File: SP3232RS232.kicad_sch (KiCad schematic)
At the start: 14 parts, among them J13 RSS232Out, J14 RSS232In, U4 MAX3232

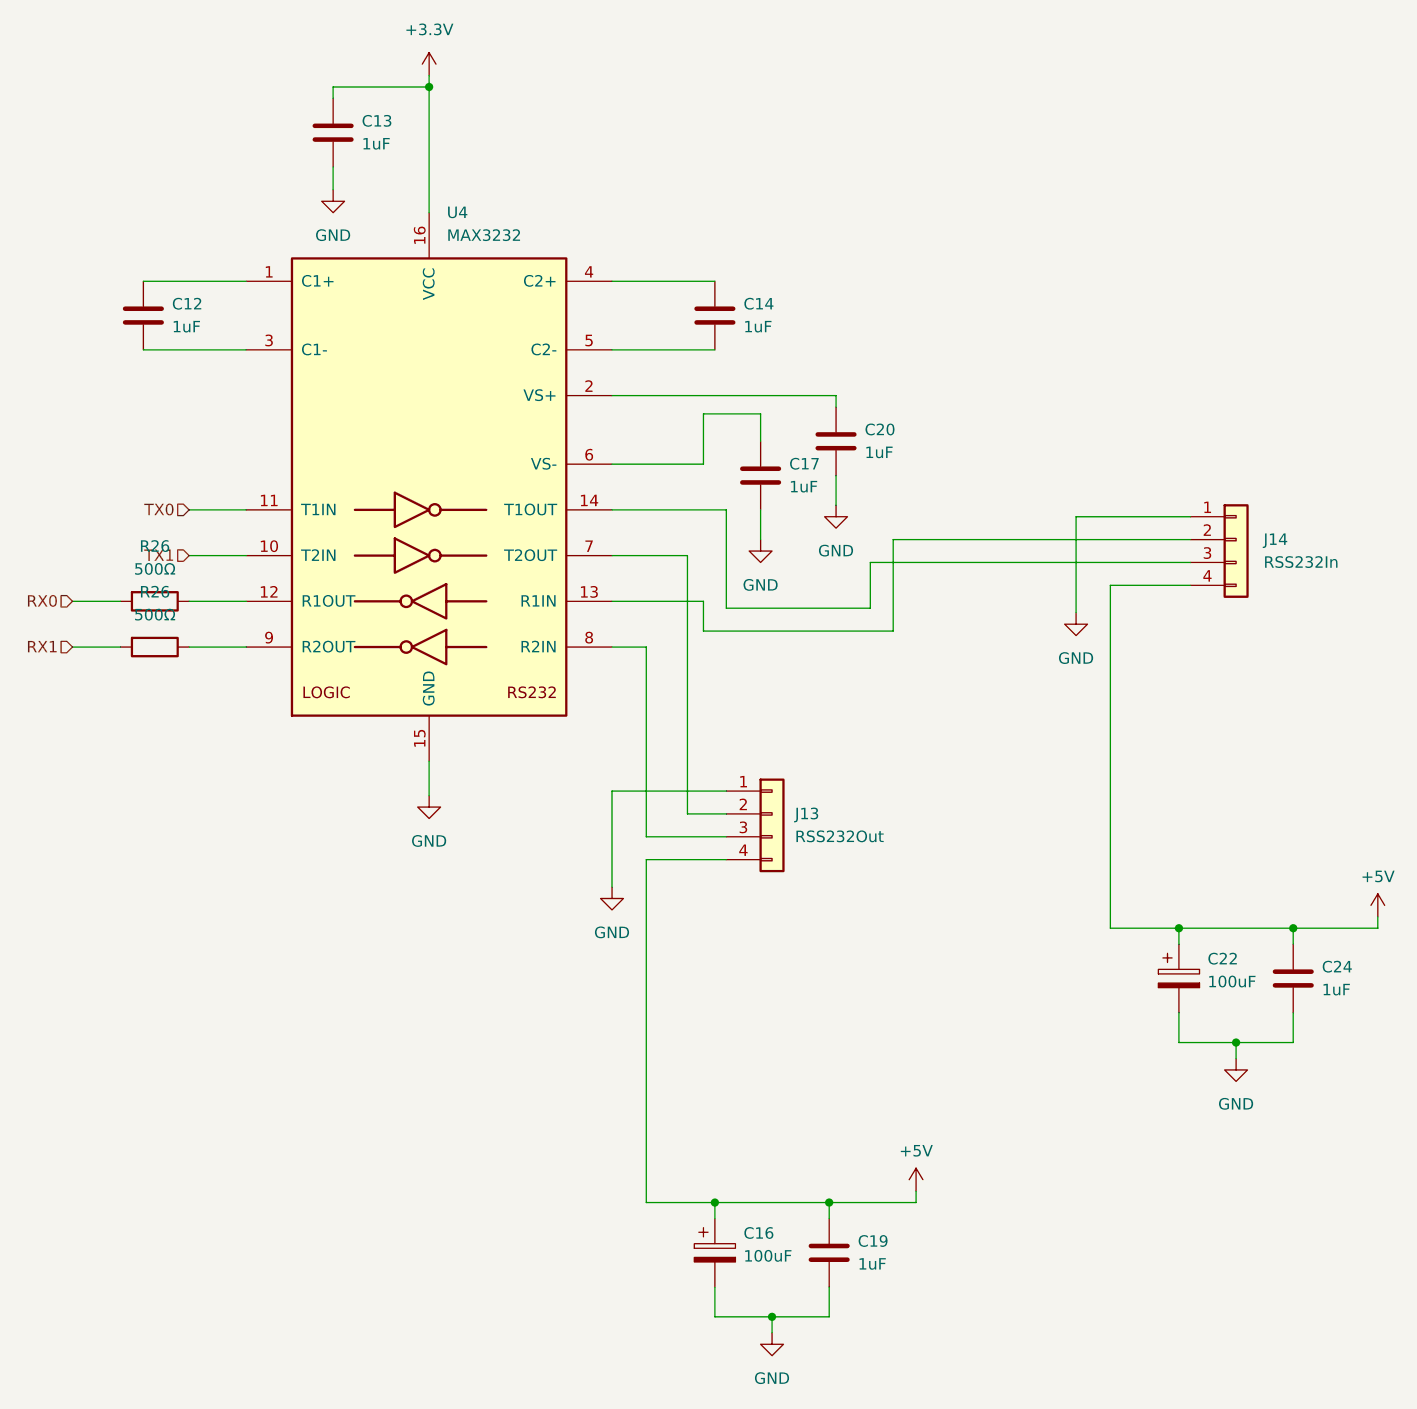
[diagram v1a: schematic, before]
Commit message: Finished schematic. Move to PCB.
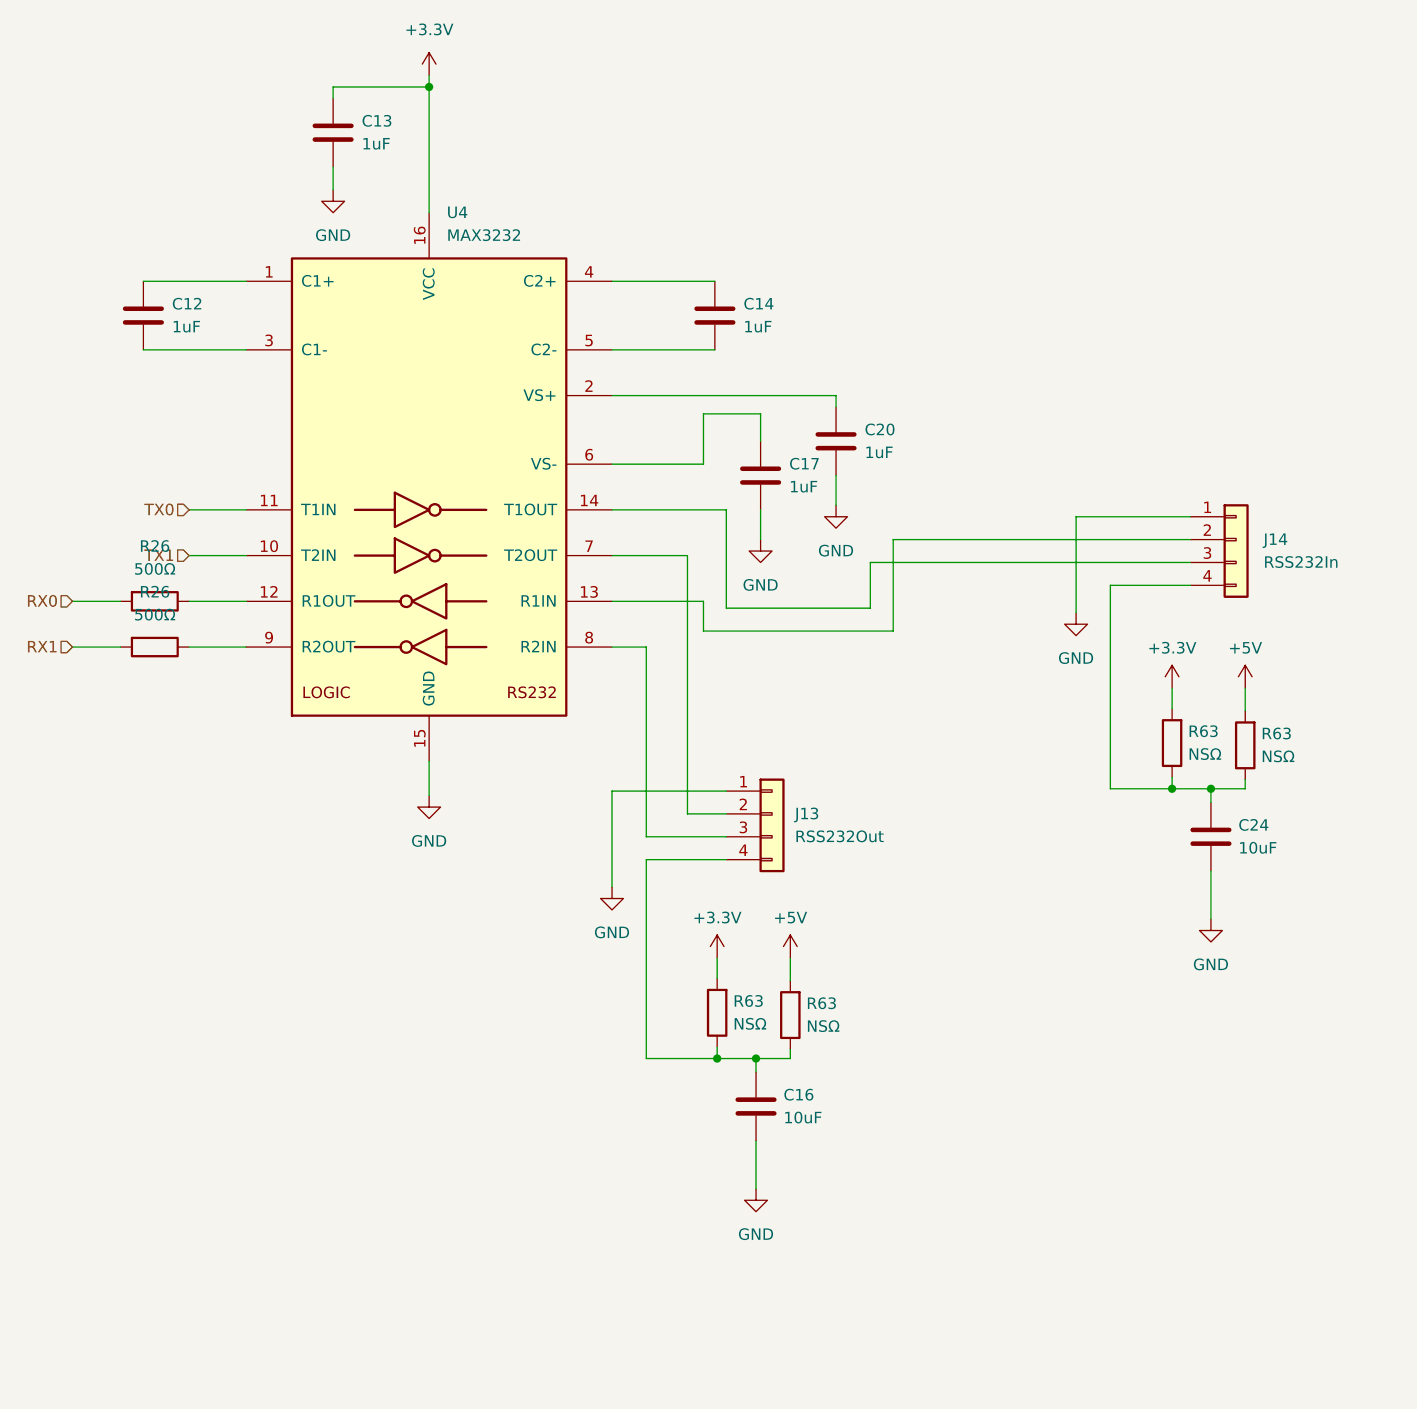
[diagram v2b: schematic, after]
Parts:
- removed C16, C22: 100uF, Capacitor_SMD:CP_Elec_8x11.9, symbol Device:C_Polarized
- removed C19: 1uF, Capacitor_SMD:C_0805_2012Metric, symbol Device:C
- added C16: 10uF, Capacitor_SMD:C_0805_2012Metric, symbol Device:C
- added R63 (x4): NSΩ, Resistor_SMD:R_0805_2012Metric, symbol Device:R
- C24: value 1uF -> 10uF
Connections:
- net +3.3V: now also R63.2, R63.2
- net +5V: now also R63.2, R63.2; no longer C24.1, J13.4 (Pin_4), J14.4 (Pin_4)
- net GND: now also C16.2
- new net: C16.1, J13.4 (Pin_4), R63.1, R63.1
- new net: C24.1, J14.4 (Pin_4), R63.1, R63.1
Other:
- moved on the sheet: C24
